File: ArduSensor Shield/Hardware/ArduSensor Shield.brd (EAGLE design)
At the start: 61 x 53.3 mm, 23 parts

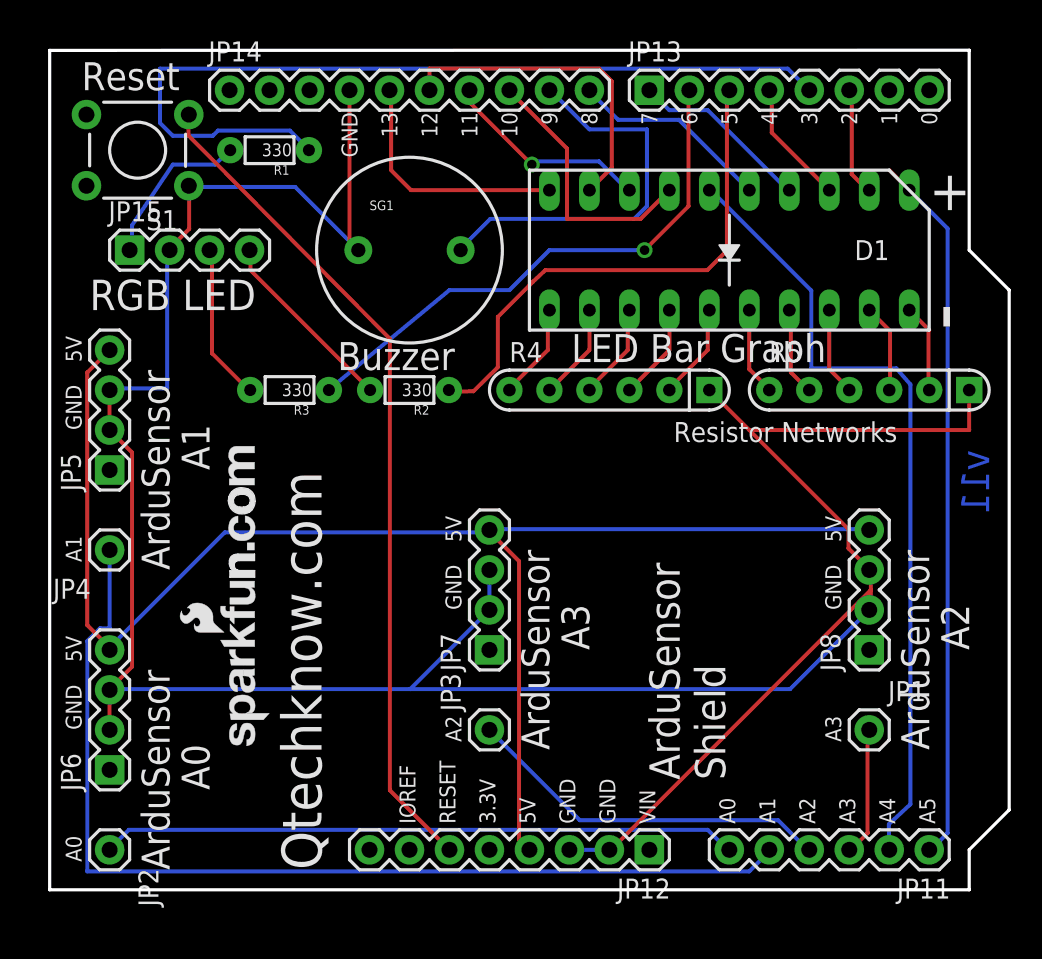
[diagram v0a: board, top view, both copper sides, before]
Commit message: Adding Shield hardware version 1.2
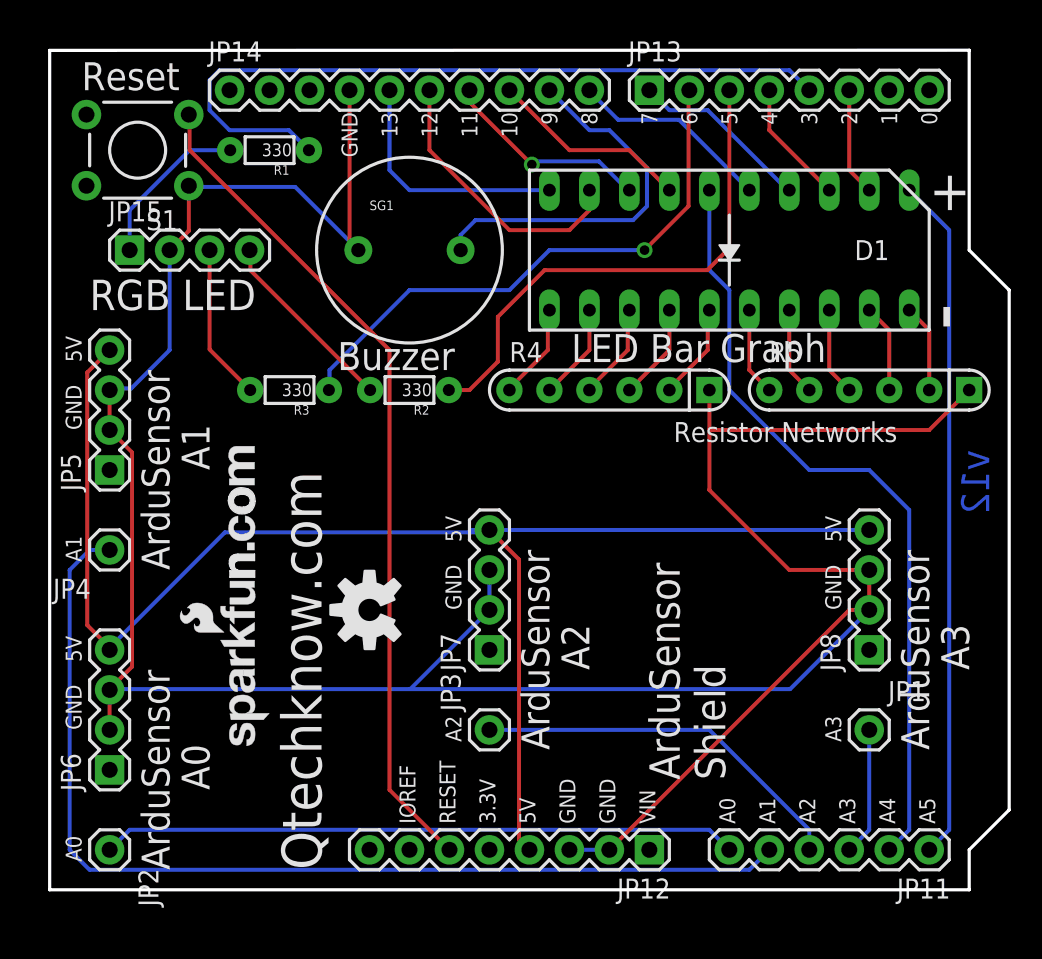
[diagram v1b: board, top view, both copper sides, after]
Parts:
- added LOGO1: OSHW-LOGOM, SparkFun-Aesthetics:OSHW-LOGO-M
- moved FRAME1 15.5 mm to (6.35, -10.2)
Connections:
- net A0: now also JP11.6, JP2.1; no longer D1.1, JP11.1
- net A1: now also JP11.5, JP4.1; no longer D1.6, JP11.2
- net A2: now also JP11.4, JP3.1; no longer JP1.1, JP11.3
- net A3: now also JP1.1, JP11.3; no longer JP11.4, JP3.1
- net A4: now also D1.6, JP11.2; no longer JP11.5, JP4.1
- net A5: now also D1.1, JP11.1; no longer JP11.6, JP2.1
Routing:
- net A2: track 8.22 -> 24.2 mm
- net A4: track 65.3 -> 49.9 mm
- net A1: track 51.0 -> 66.3 mm
- net A3: track 23.5 -> 8.15 mm
- net D3: track 55.7 -> 48.2 mm
- net A0: track 45.2 -> 40.4 mm
- net D10: track 17.0 -> 12.8 mm
- net A5: track 40.4 -> 43.5 mm
- net D12: track 20.8 -> 17.9 mm
- net GND: track 183.9 -> 186.0 mm
- net 5V: track 93.1 -> 94.5 mm
- net D6: track 34.7 -> 35.8 mm
- net D9: track 25.1 -> 24.2 mm
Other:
- board text added: "v12"
- board text removed: "v11"
